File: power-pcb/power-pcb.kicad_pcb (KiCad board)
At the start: 2 copper layers, 75 x 55 mm, 41 parts, among them J1 Network Connector, J2 STDC14, SW1 SW_Push, U1 LD39050PU33R, U2 STM32G474RBT6, U3 SN65HVD230, Y1 8MHz

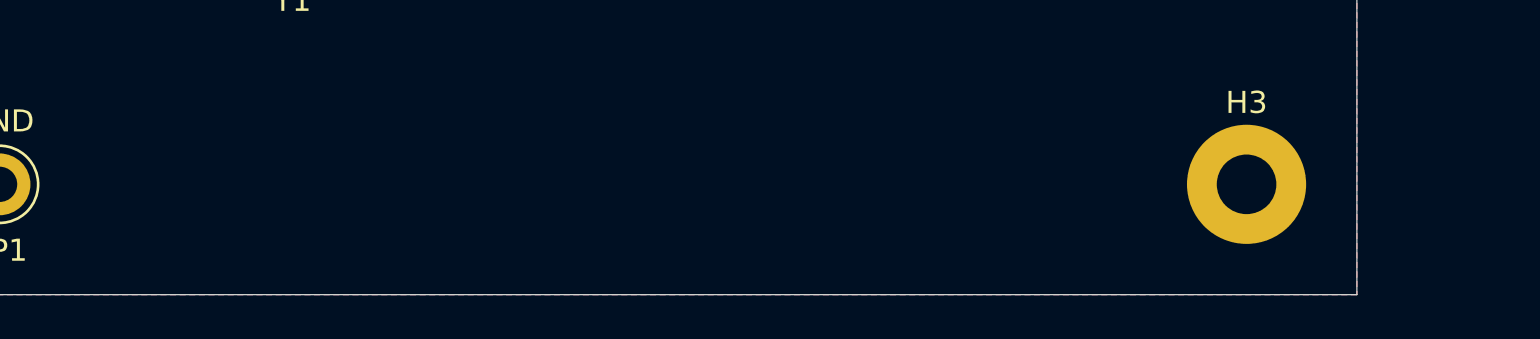
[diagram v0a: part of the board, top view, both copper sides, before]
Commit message: power-pcb: update project metadata
Also added project code, name and version to silkscreen in the board
layout.
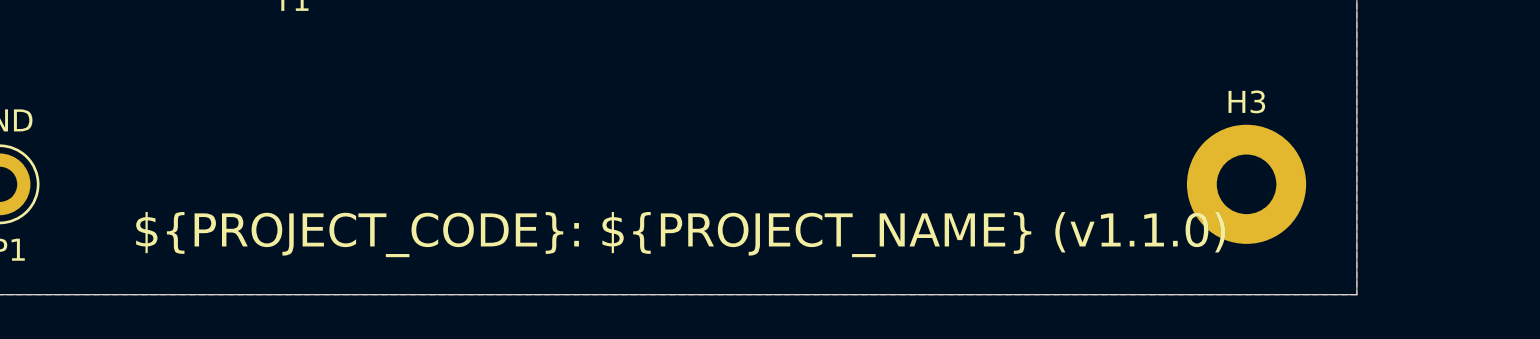
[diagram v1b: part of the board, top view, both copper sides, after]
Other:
- board text added: "${PROJECT_CODE}: ${PROJECT_NAME} (${REVISION})"
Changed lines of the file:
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@@
 	(paper "A4")
 	(title_block
-		(title "Base board layout")
-		(date "2025-04-06")
-		(rev "v1.0.0")
+		(title "Board layout")
+		(date "2026-03-28")
+		(rev "v1.1.0")
 	)
 	(layers
@@
 		)
 	)
-	(property "AUTHOR" "Guillaume Chénier")
-	(property "CONTRIBUTORS" "Eliot F., Wilfred P.")
-	(property "PROJECT_CODE" "TEM.00")
-	(property "PROJECT_NAME" "STM32 PCB Template")
-	(property "REVIEWERS" "Eliot F.")
+	(property "AUTHOR" "Daphné H.")
+	(property "CONTRIBUTORS" "")
+	(property "PROJECT_CODE" "PCB.04")
+	(property "PROJECT_NAME" "Power Control PCB")
+	(property "REVIEWERS" "")
 	(net 0 "")
 	(net 1 "GND")
@@
 		(layer "Edge.Cuts")
 	)
+	(gr_text "${PROJECT_CODE}: ${PROJECT_NAME} (${REVISION})"
+		(at 209.5 74.5 0)
+		(layer "F.SilkS")
+		(effects
+			(font
+				(size 1.5 1.5)
+				(thickness 0.1875)
+			)
+			(justify left bottom)
+		)
+	)
 	(segment

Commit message: power-pcb: re-annotate schematic and start board
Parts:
- added C18: 10n, Capacitor_SMD:C_0402_1005Metric_Pad0.74x0.62mm_HandSolder, F.Cu at (94.4, 134.0)
- added C19: 100n, Capacitor_SMD:C_0603_1608Metric_Pad1.08x0.95mm_HandSolder, F.Cu at (89.9, 122.3)
- added C20: 100n, Capacitor_SMD:C_0603_1608Metric_Pad1.08x0.95mm_HandSolder, F.Cu at (89.9, 124.8)
- added C21: 100n, Capacitor_SMD:C_0603_1608Metric_Pad1.08x0.95mm_HandSolder, F.Cu at (89.9, 127.3)
- added C22: 2.2u, Capacitor_SMD:C_0805_2012Metric_Pad1.18x1.45mm_HandSolder, F.Cu at (82.0, 134.5)
- added C23: 2.2u, Capacitor_SMD:C_0805_2012Metric_Pad1.18x1.45mm_HandSolder, F.Cu at (82.0, 137.5)
- added C24: 2.2u, Capacitor_SMD:C_0805_2012Metric_Pad1.18x1.45mm_HandSolder, F.Cu at (82.0, 140.6)
- added C25: 30p, Capacitor_SMD:C_0603_1608Metric_Pad1.08x0.95mm_HandSolder, F.Cu at (89.9, 129.8)
- added C26: 30p, Capacitor_SMD:C_0603_1608Metric_Pad1.08x0.95mm_HandSolder, F.Cu at (94.2, 117.3)
- added C27: 100n, Capacitor_SMD:C_0603_1608Metric_Pad1.08x0.95mm_HandSolder, F.Cu at (101.0, 64.7)
- added C28: 100n, Capacitor_SMD:C_0603_1608Metric_Pad1.08x0.95mm_HandSolder, F.Cu at (101.0, 67.2)
- added C29: 100n, Capacitor_SMD:C_0603_1608Metric_Pad1.08x0.95mm_HandSolder, F.Cu at (101.0, 69.7)
- added C30: 100n, Capacitor_SMD:C_0603_1608Metric_Pad1.08x0.95mm_HandSolder, F.Cu at (101.0, 72.2)
- added C31: 100n, Capacitor_SMD:C_0603_1608Metric_Pad1.08x0.95mm_HandSolder, F.Cu at (101.0, 74.7)
- added C32: 100n, Capacitor_SMD:C_0603_1608Metric_Pad1.08x0.95mm_HandSolder, F.Cu at (101.0, 77.2)
- added C33: 100n, Capacitor_SMD:C_0603_1608Metric_Pad1.08x0.95mm_HandSolder, F.Cu at (101.0, 79.8)
- added C34: 100n, Capacitor_SMD:C_0603_1608Metric_Pad1.08x0.95mm_HandSolder, F.Cu at (101.0, 82.3)
- added C35: 100n, Capacitor_SMD:C_0603_1608Metric_Pad1.08x0.95mm_HandSolder, F.Cu at (120.8, 130.3)
- added C36: 10u, Capacitor_SMD:C_1206_3216Metric_Pad1.33x1.80mm_HandSolder, F.Cu at (131.5, 128.3)
- added C37: 10u, Capacitor_SMD:C_1206_3216Metric_Pad1.33x1.80mm_HandSolder, F.Cu at (131.5, 131.6)
- added C38: 100n, Capacitor_SMD:C_0603_1608Metric_Pad1.08x0.95mm_HandSolder, F.Cu at (145.8, 111.0)
- added C39: 100n, Capacitor_SMD:C_0603_1608Metric_Pad1.08x0.95mm_HandSolder, F.Cu at (145.8, 113.5)
- added C40: 10n, Capacitor_SMD:C_0402_1005Metric_Pad0.74x0.62mm_HandSolder, F.Cu at (167.1, 119.5)
- added C41: 10n, Capacitor_SMD:C_0402_1005Metric_Pad0.74x0.62mm_HandSolder, F.Cu at (167.1, 121.5)
- added C42: 10n, Capacitor_SMD:C_0402_1005Metric_Pad0.74x0.62mm_HandSolder, F.Cu at (167.1, 123.4)
- added C43: 10n, Capacitor_SMD:C_0402_1005Metric_Pad0.74x0.62mm_HandSolder, F.Cu at (167.1, 125.4)
- added C44: 100n, Capacitor_SMD:C_0603_1608Metric_Pad1.08x0.95mm_HandSolder, F.Cu at (145.1, 160.5)
- added C45: 100n, Capacitor_SMD:C_0603_1608Metric_Pad1.08x0.95mm_HandSolder, F.Cu at (145.1, 163.0)
- added C46: 10n, Capacitor_SMD:C_0402_1005Metric_Pad0.74x0.62mm_HandSolder, F.Cu at (166.5, 169.0)
- added C47: 10n, Capacitor_SMD:C_0402_1005Metric_Pad0.74x0.62mm_HandSolder, F.Cu at (166.5, 170.9)
- added C48: 10n, Capacitor_SMD:C_0402_1005Metric_Pad0.74x0.62mm_HandSolder, F.Cu at (166.5, 172.9)
- added C49: 10n, Capacitor_SMD:C_0402_1005Metric_Pad0.74x0.62mm_HandSolder, F.Cu at (166.5, 174.9)
- added C50: 10u, Capacitor_SMD:C_1206_3216Metric_Pad1.33x1.80mm_HandSolder, F.Cu at (82.6, 171.0)
- added C51: 10u, Capacitor_SMD:C_1206_3216Metric_Pad1.33x1.80mm_HandSolder, F.Cu at (82.6, 174.4)
- added C52: 10u, Capacitor_SMD:C_1206_3216Metric_Pad1.33x1.80mm_HandSolder, F.Cu at (82.6, 177.7)
- added C53: 100p, Capacitor_SMD:C_0402_1005Metric_Pad0.74x0.62mm_HandSolder, F.Cu at (107.2, 179.0)
- added C54: 100n, Capacitor_SMD:C_0603_1608Metric_Pad1.08x0.95mm_HandSolder, F.Cu at (87.8, 170.6)
- added C55: 100n, Capacitor_SMD:C_0603_1608Metric_Pad1.08x0.95mm_HandSolder, F.Cu at (87.8, 173.1)
- added C56: 100n, Capacitor_SMD:C_0603_1608Metric_Pad1.08x0.95mm_HandSolder, F.Cu at (129.2, 169.2)
- added C57: 100n, Capacitor_SMD:C_0603_1608Metric_Pad1.08x0.95mm_HandSolder, F.Cu at (129.2, 171.7)
- added C58: 100n, Capacitor_SMD:C_0603_1608Metric_Pad1.08x0.95mm_HandSolder, F.Cu at (129.2, 147.0)
- added C59: 100n, Capacitor_SMD:C_0603_1608Metric_Pad1.08x0.95mm_HandSolder, F.Cu at (129.2, 149.5)
- added C60: 100n, Capacitor_SMD:C_0603_1608Metric_Pad1.08x0.95mm_HandSolder, F.Cu at (158.6, 147.0)
- added C61: 100n, Capacitor_SMD:C_0603_1608Metric_Pad1.08x0.95mm_HandSolder, F.Cu at (158.6, 149.5)
- added C62: 100n, Capacitor_SMD:C_0603_1608Metric_Pad1.08x0.95mm_HandSolder, F.Cu at (29.7, 67.4)
- added C63: 100n, Capacitor_SMD:C_0603_1608Metric_Pad1.08x0.95mm_HandSolder, F.Cu at (29.7, 70.0)
- added C64: 100n, Capacitor_SMD:C_0603_1608Metric_Pad1.08x0.95mm_HandSolder, F.Cu at (29.7, 72.5)
- added C65: 100n, Capacitor_SMD:C_0603_1608Metric_Pad1.08x0.95mm_HandSolder, F.Cu at (29.7, 75.0)
- added C66: 100n, Capacitor_SMD:C_0603_1608Metric_Pad1.08x0.95mm_HandSolder, F.Cu at (29.7, 77.5)
- added C67: 100n, Capacitor_SMD:C_0603_1608Metric_Pad1.08x0.95mm_HandSolder, F.Cu at (29.7, 80.0)
- added D10: YELLOW, Exocet:LED_0805_2012Metric_With_Annotations, F.Cu at (98.6, 140.5)
- added D11: SMF5.0A, Diode_SMD:D_SOD-123F, F.Cu at (88.4, 178.5)
- added D12: SMF5.0A, Diode_SMD:D_SOD-123F, F.Cu at (91.6, 85.7)
- added D13: SMF5.0A, Diode_SMD:D_SOD-123F, F.Cu at (91.6, 89.0)
- added D14: SMF24CA, Diode_SMD:D_SOD-123F, F.Cu at (91.6, 92.4)
- added D15: SMF24CA, Diode_SMD:D_SOD-123F, F.Cu at (91.6, 95.7)
- added D16: SMF28A, Diode_SMD:D_SMF, F.Cu at (91.7, 99.1)
- added D17: SMF28A, Diode_SMD:D_SMF, F.Cu at (91.7, 102.4)
- added D18: 1N4148, Diode_THT:D_DO-35_SOD27_P7.62mm_Horizontal, F.Cu at (46.5, 98.9)
- added D19: 1N4148, Diode_THT:D_DO-35_SOD27_P7.62mm_Horizontal, F.Cu at (46.5, 102.4)
- added D20: BZX79-C4V7, Diode_THT:D_DO-35_SOD27_P7.62mm_Horizontal, F.Cu at (46.5, 106.0)
- added D3: GREEN, Exocet:LED_0805_2012Metric_With_Annotations, F.Cu at (70.6, 120.3)
- added D4: GREEN, Exocet:LED_0805_2012Metric_With_Annotations, F.Cu at (70.6, 123.4)
- added D5: GREEN, Exocet:LED_0805_2012Metric_With_Annotations, F.Cu at (70.6, 126.4)
- added D6: SMF24CA, Diode_SMD:D_SOD-123F, F.Cu at (72.4, 140.6)
- added D7: SMF24CA, Diode_SMD:D_SOD-123F, F.Cu at (72.4, 143.9)
- added D8: SS34, Diode_SMD:D_SMA, F.Cu at (63.1, 135.8)
- added D9: SMF5.0A, Diode_SMD:D_SOD-123F, F.Cu at (72.4, 147.3)
- added F2: 5A, Exocet:Fuseholder_Littelfuse_Combined, F.Cu at (39.7, 114.3)
- added F3: RUEF110, Fuse:Fuse_Littelfuse_395Series, F.Cu at (34.3, 147.7)
- added F4: 10A, Exocet:Fuseholder_Littelfuse_Combined, F.Cu at (57.1, 70.7)
- added J10: USB_A, Connector_USB:USB_A_Molex_67643_Horizontal, F.Cu at (98.2, 147.4)
- added J11: Screw_Terminal_01x04, Exocet:Wuerth_Term_Blk_4pos_Side_Entry_5mm, F.Cu at (122.8, 163.3)
- added J12: Screw_Terminal_01x04, Exocet:Wuerth_Term_Blk_4pos_Side_Entry_5mm, F.Cu at (122.8, 141.1)
- added J13: Screw_Terminal_01x04, Exocet:Wuerth_Term_Blk_4pos_Side_Entry_5mm, F.Cu at (152.3, 141.1)
- added J14: Screw_Terminal_01x02, Exocet:Wuerth_Term_Blk_2pos_Side_Entry_5mm, F.Cu at (31.8, 90.4)
- added J15: Screw_Terminal_01x06, Exocet:Wuerth_Term_Blk_6pos_Side_Entry_5mm, F.Cu at (67.9, 46.1)
- added J16: Screw_Terminal_01x02, Exocet:Wuerth_Term_Blk_2pos_Side_Entry_5mm, F.Cu at (31.8, 99.1)
- added J17: Screw_Terminal_01x04, Exocet:Wuerth_Term_Blk_4pos_Side_Entry_5mm, F.Cu at (71.4, 79.4)
- added J18: Screw_Terminal_01x03, Exocet:Wuerth_Term_Blk_3pos_Side_Entry_5mm, F.Cu at (67.9, 54.9)
- added J3: STDC14, Connector_PinHeader_1.27mm:PinHeader_2x07_P1.27mm_Vertical_SMD, F.Cu at (36.7, 155.9)
- added J4: USB_C_Receptacle_USB2.0_16P, Connector_USB:USB_C_Receptacle_GCT_USB4085, F.Cu at (52.0, 150.1)
- added J5: RA25S, Connector_Dsub:DSUB-25_Socket_Horizontal_P2.77x2.84mm_EdgePinOffset7.70mm_Housed_MountingHolesOffset9.12mm, F.Cu at (143.0, 45.3)
- added J6: JST PH, Connector_JST:JST_PH_S3B-PH-K_1x03_P2.00mm_Horizontal, F.Cu at (121.6, 112.1)
- added J7: JST PH, Connector_JST:JST_PH_S3B-PH-K_1x03_P2.00mm_Horizontal, F.Cu at (121.6, 121.8)
- added J8: Screw_Terminal_01x03, Exocet:Wuerth_Term_Blk_3pos_Side_Entry_5mm, F.Cu at (152.2, 113.9)
- added J9: Screw_Terminal_01x03, Exocet:Wuerth_Term_Blk_3pos_Side_Entry_5mm, F.Cu at (151.6, 163.3)
- added JP1: Jumper_3_Bridged12, Connector_PinHeader_2.54mm:PinHeader_1x03_P2.54mm_Vertical, F.Cu at (51.5, 141.2)
- added JP2: Jumper_3_Bridged12, Connector_PinHeader_2.54mm:PinHeader_1x03_P2.54mm_Vertical, F.Cu at (56.1, 141.2)
- added JP3: Jumper_3_Bridged12, Connector_PinHeader_2.54mm:PinHeader_1x03_P2.54mm_Vertical, F.Cu at (60.7, 141.2)
- added JP4: Jumper_3_Bridged12, Connector_PinHeader_2.54mm:PinHeader_1x03_P2.54mm_Vertical, F.Cu at (109.2, 132.8)
- added JP5: SolderJumper_2_Open, Jumper:SolderJumper-2_P1.3mm_Open_RoundedPad1.0x1.5mm, F.Cu at (107.7, 173.0)
- added JP6: SolderJumper_2_Bridged, Jumper:SolderJumper-2_P1.3mm_Bridged_Pad1.0x1.5mm, F.Cu at (91.0, 105.9)
- added L1: 10u, Inductor_THT:L_Radial_D8.7mm_P5.00mm_Fastron_07HCP, F.Cu at (34.5, 124.0)
- added L2: 10u, Inductor_THT:L_Radial_D8.7mm_P5.00mm_Fastron_07HCP, F.Cu at (34.5, 134.2)
- added L3: GZ2012D101TF, Inductor_SMD:L_0805_2012Metric_Pad1.05x1.20mm_HandSolder, F.Cu at (72.1, 150.3)
- added L4: GZ2012D101TF, Inductor_SMD:L_0805_2012Metric_Pad1.05x1.20mm_HandSolder, F.Cu at (158.8, 130.0)
- added L5: GZ2012D101TF, Inductor_SMD:L_0805_2012Metric_Pad1.05x1.20mm_HandSolder, F.Cu at (158.8, 132.7)
- added L6: GZ2012D101TF, Inductor_SMD:L_0805_2012Metric_Pad1.05x1.20mm_HandSolder, F.Cu at (158.2, 179.4)
- added L7: GZ2012D101TF, Inductor_SMD:L_0805_2012Metric_Pad1.05x1.20mm_HandSolder, F.Cu at (158.2, 182.2)
- added L8: GZ2012D101TF, Inductor_SMD:L_0805_2012Metric_Pad1.05x1.20mm_HandSolder, F.Cu at (108.0, 169.8)
- added Q1: AO3400A, Package_TO_SOT_SMD:SOT-23, F.Cu at (71.8, 68.4)
- added Q2: AO3400A, Package_TO_SOT_SMD:SOT-23, F.Cu at (71.8, 72.9)
- added Q3: AO3400A, Package_TO_SOT_SMD:SOT-23, F.Cu at (76.7, 68.4)
- added Q4: AO3400A, Package_TO_SOT_SMD:SOT-23, F.Cu at (76.7, 72.9)
- added Q5: AO3400A, Package_TO_SOT_SMD:SOT-23, F.Cu at (81.6, 68.4)
- added Q6: AO3400A, Package_TO_SOT_SMD:SOT-23, F.Cu at (81.6, 72.9)
- added Q7: AO3400A, Package_TO_SOT_SMD:SOT-23, F.Cu at (86.5, 68.4)
- added Q8: AO3400A, Package_TO_SOT_SMD:SOT-23, F.Cu at (86.5, 72.9)
- added R10: 2.7k, Resistor_SMD:R_0603_1608Metric_Pad0.98x0.95mm_HandSolder, F.Cu at (94.2, 119.8)
- added R11: 2.7k, Resistor_SMD:R_0603_1608Metric_Pad0.98x0.95mm_HandSolder, F.Cu at (94.2, 122.3)
- added R12: 47, Resistor_SMD:R_0603_1608Metric_Pad0.98x0.95mm_HandSolder, F.Cu at (94.2, 124.8)
- added R13: 10k, Resistor_SMD:R_0603_1608Metric_Pad0.98x0.95mm_HandSolder, F.Cu at (94.2, 127.3)
- added R14: 1k, Resistor_SMD:R_0402_1005Metric_Pad0.72x0.64mm_HandSolder, F.Cu at (94.4, 139.6)
- added R15: 2.2k, Resistor_SMD:R_0603_1608Metric_Pad0.98x0.95mm_HandSolder, F.Cu at (120.8, 132.8)
- added R16: 82k, Resistor_SMD:R_0603_1608Metric_Pad0.98x0.95mm_HandSolder, F.Cu at (145.8, 116.0)
- added R17: 6.8k, Resistor_SMD:R_0603_1608Metric_Pad0.98x0.95mm_HandSolder, F.Cu at (145.8, 118.6)
- added R18: 10k, Resistor_SMD:R_0603_1608Metric_Pad0.98x0.95mm_HandSolder, F.Cu at (145.8, 121.1)
- added R19: 10k, Resistor_SMD:R_0603_1608Metric_Pad0.98x0.95mm_HandSolder, F.Cu at (145.8, 123.6)
- added R20: 2.7k, Resistor_SMD:R_0603_1608Metric_Pad0.98x0.95mm_HandSolder, F.Cu at (145.8, 126.1)
- added R21: 2.7k, Resistor_SMD:R_0603_1608Metric_Pad0.98x0.95mm_HandSolder, F.Cu at (145.8, 128.6)
- added R22: 82k, Resistor_SMD:R_0603_1608Metric_Pad0.98x0.95mm_HandSolder, F.Cu at (145.1, 165.5)
- added R23: 6.8k, Resistor_SMD:R_0603_1608Metric_Pad0.98x0.95mm_HandSolder, F.Cu at (145.1, 168.0)
- added R24: 10k, Resistor_SMD:R_0603_1608Metric_Pad0.98x0.95mm_HandSolder, F.Cu at (145.1, 170.5)
- added R25: 10k, Resistor_SMD:R_0603_1608Metric_Pad0.98x0.95mm_HandSolder, F.Cu at (145.1, 173.0)
- added R26: 2.7k, Resistor_SMD:R_0603_1608Metric_Pad0.98x0.95mm_HandSolder, F.Cu at (145.1, 175.5)
- added R27: 2.7k, Resistor_SMD:R_0603_1608Metric_Pad0.98x0.95mm_HandSolder, F.Cu at (145.1, 178.0)
- added R28: 10k, Resistor_SMD:R_0603_1608Metric_Pad0.98x0.95mm_HandSolder, F.Cu at (87.8, 175.6)
- added R29: 10k, Resistor_SMD:R_0603_1608Metric_Pad0.98x0.95mm_HandSolder, F.Cu at (29.7, 82.5)
- added R30: 10k, Resistor_SMD:R_0603_1608Metric_Pad0.98x0.95mm_HandSolder, F.Cu at (29.7, 85.0)
- added R31: 3.6k, Resistor_SMD:R_0603_1608Metric_Pad0.98x0.95mm_HandSolder, F.Cu at (34.0, 67.4)
- added R32: 120, Resistor_THT:R_Axial_DIN0309_L9.0mm_D3.2mm_P12.70mm_Horizontal, F.Cu at (82.6, 53.1)
- added R33: 120, Resistor_THT:R_Axial_DIN0309_L9.0mm_D3.2mm_P12.70mm_Horizontal, F.Cu at (82.6, 57.9)
- added R34: 6.8k, Resistor_SMD:R_0603_1608Metric_Pad0.98x0.95mm_HandSolder, F.Cu at (34.0, 70.0)
- added R35: 10k, Resistor_SMD:R_0603_1608Metric_Pad0.98x0.95mm_HandSolder, F.Cu at (34.0, 72.5)
- added R36: 10k, Resistor_SMD:R_0603_1608Metric_Pad0.98x0.95mm_HandSolder, F.Cu at (34.0, 75.0)
- added R37: 10k, Resistor_SMD:R_0603_1608Metric_Pad0.98x0.95mm_HandSolder, F.Cu at (34.0, 77.5)
- added R38: 10k, Resistor_SMD:R_0603_1608Metric_Pad0.98x0.95mm_HandSolder, F.Cu at (34.0, 80.0)
- added R39: 10k, Resistor_SMD:R_0603_1608Metric_Pad0.98x0.95mm_HandSolder, F.Cu at (34.0, 82.5)
- added R40: 10k, Resistor_SMD:R_0603_1608Metric_Pad0.98x0.95mm_HandSolder, F.Cu at (34.0, 85.0)
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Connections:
- C1 pad 1: +5V -> Net-(U1-BOOT)
- C1 pad 2: GND -> Net-(D2-K)
- C10 pad 1: +3.3V -> +5V
- C15 pad 1: /STM32 Base Layout/OSC_IN -> +3.3V
- C16 pad 1: /STM32 Base Layout/OSC_OUT -> GND
- C16 pad 2: GND -> +3.3V
- C17 pad 1: GND -> +3.3V
- C17 pad 2: /STM32 Base Layout/T_NRST -> GND
- C2 pad 1: GND -> +24V
- C2 pad 2: +3.3V -> GND
- C3 pad 1: GND -> Net-(C3-Pad1)
- C3 pad 2: +3.3V -> GND
- C4 pad 1: +5V -> Net-(C3-Pad1)
- C5 pad 1: +3.3V -> +24V
- C6 pad 1: +3.3V -> Net-(D9-K)
- C7 pad 1: +3.3V -> Net-(C7-Pad1)
- C9 pad 1: +3.3V -> +5V
- D1 pad 1: GND -> +24V
- D1 pad 2: Net-(D1-A) -> GND
- D2 pad 1: GND -> Net-(D2-K)
- D2 pad 2: Net-(D2-A) -> GND
- F1 pad 1: Net-(J1-+5V) -> Net-(C3-Pad1)
- F1 pad 2: +5V -> /Non-Isolated Interfaces and Power/5V_NETWORK
- J1 pad 1: +24V -> Net-(J1-+24V)
- J1 pad 2: Net-(J1-+5V) -> unconnected-(J1-+5V-Pad2)
- J1 pad 3: /STM32 Base Layout/CAN_L -> /Non-Isolated Interfaces and Power/CAN_L
- J1 pad 4: /STM32 Base Layout/CAN_H -> /Non-Isolated Interfaces and Power/CAN_H
- J2 pad 1: unconnected-(J2-NC-Pad1) -> +24V
- J2 pad 2: unconnected-(J2-NC-Pad2) -> GND
- R1 pad 1: Net-(U2-PB8) -> Net-(C3-Pad1)
- R1 pad 2: GND -> Net-(U1-VSENSE)
- R2 pad 1: Net-(U2-PA15) -> +24V
- R2 pad 2: /STM32 Base Layout/T_JTDI -> Net-(D3-A)
- R3 pad 1: Net-(U3-Rs) -> +5V
- R3 pad 2: GND -> Net-(D4-A)
- R4 pad 2: Net-(D1-A) -> Net-(D5-A)
- R5 pad 1: /STM32 Base Layout/STATUS_LED -> Net-(U1-VSENSE)
- R5 pad 2: Net-(D2-A) -> Net-(R5-Pad2)
- SW1 pad 1: /STM32 Base Layout/T_NRST -> /Non-Isolated Interfaces and Power/~{RST}
- TP1 pad 1: GND -> Net-(C3-Pad1)
- TP2 pad 1: /STM32 Base Layout/CAN_RX -> +24V
- TP3 pad 1: +5V -> GND
- TP4 pad 1: /STM32 Base Layout/CAN_TX -> Net-(U1-VSENSE)
- TP5 pad 1: +3.3V -> Net-(C7-Pad1)
- U1 pad 1: +5V -> Net-(U1-BOOT)
- U1 pad 2: GND -> unconnected-(U1-NC-Pad2)
- U1 pad 4: +3.3V -> Net-(U1-VSENSE)
- U1 pad 6: +5V -> GND
- U1 pad 7: GND -> +24V
- U2 pad 1: +3.3V -> Net-(U2-D+_in)
- U2 pad 2: unconnected-(U2-PC13-Pad2) -> Net-(U2-D-_in)
- U2 pad 3: unconnected-(U2-PC14-Pad3) -> GND
- U2 pad 5: /STM32 Base Layout/OSC_IN -> /Non-Isolated Interfaces and Power/PC_D-
- U2 pad 6: /STM32 Base Layout/OSC_OUT -> /Non-Isolated Interfaces and Power/PC_D+
- U3 pad 1: /STM32 Base Layout/CAN_TX -> GND
- U3 pad 2: GND -> +3.3V
- U3 pad 3: +3.3V -> +5V
- Y1 pad 1: /STM32 Base Layout/OSC_IN -> /STM32 Microcontroller/OSC_IN
- Y1 pad 2: /STM32 Base Layout/OSC_OUT -> /STM32 Microcontroller/OSC_OUT
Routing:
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- removed copper zone on B.Cu, net +3.3V
- removed copper zone on F.Cu, net GND
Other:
- board outline removed

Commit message: power-pcb: fix schematic after review
- Add footprint for resitive load for the RECOM
- Add Opamps when useful
- Add capacitor and change some footprint sizes
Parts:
- removed R33: 120, Resistor_THT:R_Axial_DIN0309_L9.0mm_D3.2mm_P12.70mm_Horizontal
- C2: value 10u -> 100n; footprint Capacitor_SMD:C_1206_3216Metric_Pad1.33x1.80mm_HandSolder -> Capacitor_SMD:C_0603_1608Metric_Pad1.08x0.95mm_HandSolder
- F3, JP5, TP57, TP59: moved to B.Cu
- moved H2 171.0 mm to (123.5, 30.0)
- moved J13 137.6 mm to (30.5, 77.0), turned to -90 degrees
- moved H1 136.9 mm to (31.0, 30.0)
- moved C44 134.3 mm to (276.2, 131.5)
- moved C45 134.3 mm to (276.2, 134.0)
- moved C60 134.3 mm to (289.7, 118.0)
- moved C61 134.3 mm to (289.7, 120.5)
- moved R22 134.3 mm to (276.2, 136.5)
- moved R23 134.3 mm to (276.2, 139.0)
- moved R24 134.3 mm to (276.2, 141.5)
- moved R25 134.3 mm to (276.2, 144.0)
- moved R26 134.3 mm to (276.2, 146.5)
- moved R27 134.3 mm to (276.2, 149.1)
- moved U25 134.3 mm to (294.5, 119.2)
- moved C16 134.3 mm to (213.1, 102.5)
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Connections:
- J17 pad 1: +24V -> /Relay Board Connection/+24V_CONTACTORS
- J17 pad 4: /Relay Board Connection/+24V_CONTACTORS -> +24V
- TP57 pad 1: Net-(U18-D+_out) -> Net-(U18-D+_in)
- TP59 pad 1: Net-(U18-D-_out) -> Net-(U18-D-_in)
- U18 pad 1: Net-(J10-D+) -> Net-(U18-D+_in)
- U18 pad 2: Net-(J10-D-) -> Net-(U18-D-_in)
- U18 pad 5: Net-(U18-D-_out) -> Net-(J10-D-)
- U18 pad 6: Net-(U18-D+_out) -> Net-(J10-D+)
- U19 pad 6: Net-(U18-D-_out) -> Net-(U18-D-_in)
- U19 pad 7: Net-(U18-D+_out) -> Net-(U18-D+_in)
- U28 pad 1: Net-(D18-A) -> Net-(J16-Pin_2)
- U28 pad 2: Net-(J16-Pin_2) -> Net-(D18-A)
- U28 pad 3: Net-(F4-Pad1) -> unconnected-(U28-Pad3)
- U28 pad 4: unconnected-(U28-Pad4) -> Net-(F4-Pad1)
- U29 pad 1: Net-(D19-A) -> Net-(J17-Pin_2)
- U29 pad 2: Net-(J17-Pin_3) -> Net-(D19-A)
- U29 pad 3: Net-(J17-Pin_2) -> unconnected-(U29-Pad3)
- U29 pad 4: unconnected-(U29-Pad4) -> Net-(J17-Pin_3)
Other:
- board outline added: 102.5 x 150 mm
- board text added: "+24V"

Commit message: power-pcb: work on part placement and JLCPCB DNP
Some of the components that were recentlt added had not been marked as
DNP for JLCPCB yet, this is now done.
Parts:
- removed the C62 at (160.8, 38.5)
- removed the D14 at (222.6, 63.4)
- removed the D15 at (222.6, 66.7)
- removed the D16 at (222.8, 70.1)
- removed the D17 at (222.8, 73.4)
- removed the J15 at (65.5, 34.0)
- removed the L2 at (165.6, 105.2)
- removed the R16 at (276.8, 87.0)
- removed the R22 at (276.2, 136.5)
- removed the TP76 at (212.3, 62.6)
- removed the TP79 at (222.1, 39.2)
- removed the TP80 at (212.3, 67.6)
- removed the TP82 at (189.3, 62.2)
- removed the U27 at (198.9, 33.9)
- added C2: 2.2u, Capacitor_SMD:C_0805_2012Metric_Pad1.18x1.45mm_HandSolder, F.Cu at (88.5, 137.7)
- added C41: 100n, Capacitor_SMD:C_0402_1005Metric_Pad0.74x0.62mm_HandSolder, F.Cu at (182.9, -27.2)
- added C48: 100n, Capacitor_SMD:C_0402_1005Metric_Pad0.74x0.62mm_HandSolder, F.Cu at (175.0, 15.9)
- added C6: 2.2u, Capacitor_SMD:C_0805_2012Metric_Pad1.18x1.45mm_HandSolder, F.Cu at (69.8, 130.2)
- added C67: 100n, Capacitor_SMD:C_0402_1005Metric_Pad0.74x0.62mm_HandSolder, F.Cu at (182.9, -16.6)
- added C72: 100n, Capacitor_SMD:C_0402_1005Metric_Pad0.74x0.62mm_HandSolder, F.Cu at (168.9, -16.3)
- added D18: SMF24CA, Diode_SMD:D_SOD-123F, F.Cu at (168.0, -26.3)
- added D19: SMF24CA, Diode_SMD:D_SOD-123F, F.Cu at (168.0, -23.0)
- added D20: SMF28A, Diode_SMD:D_SMF, F.Cu at (162.3, -26.3)
- added D21: SMF28A, Diode_SMD:D_SMF, F.Cu at (162.3, -23.0)
- added D9: SMF28A, Diode_SMD:D_SMF, F.Cu at (78.5, 146.2)
- added F3: 2A, Exocet:Fuseholder_Littelfuse_Combined, F.Cu at (84.7, 154.0)
- added J18: Screw_Terminal_01x06, Exocet:Wuerth_Term_Blk_6pos_Side_Entry_5mm, F.Cu at (65.4, 34.0)
- added L3: GZ2012D101TF, Inductor_SMD:L_0805_2012Metric_Pad1.05x1.20mm_HandSolder, F.Cu at (45.5, 99.0)
- added R15: 100, Resistor_SMD:R_0603_1608Metric_Pad0.98x0.95mm_HandSolder, F.Cu at (69.5, 78.0)
- added R19: 250, Resistor_THT:R_Axial_DIN0309_L9.0mm_D3.2mm_P12.70mm_Horizontal, F.Cu at (140.1, 16.4)
- added R20: 56k, Resistor_SMD:R_0603_1608Metric_Pad0.98x0.95mm_HandSolder, F.Cu at (175.1, -35.5)
- added R21: 5.1k, Resistor_SMD:R_0402_1005Metric_Pad0.72x0.64mm_HandSolder, F.Cu at (182.9, -29.2)
- added R25: 10k, Resistor_SMD:R_0603_1608Metric_Pad0.98x0.95mm_HandSolder, F.Cu at (175.1, -30.5)
- added R28: 100, Resistor_SMD:R_0603_1608Metric_Pad0.98x0.95mm_HandSolder, F.Cu at (175.1, -28.0)
- added R29: 56k, Resistor_SMD:R_0603_1608Metric_Pad0.98x0.95mm_HandSolder, F.Cu at (167.1, 7.58)
- added R30: 5.1k, Resistor_SMD:R_0402_1005Metric_Pad0.72x0.64mm_HandSolder, F.Cu at (175.0, 13.9)
- added R34: 10k, Resistor_SMD:R_0603_1608Metric_Pad0.98x0.95mm_HandSolder, F.Cu at (167.1, 12.6)
- added R37: 100, Resistor_SMD:R_0603_1608Metric_Pad0.98x0.95mm_HandSolder, F.Cu at (167.1, 15.1)
- added R38: 250, Resistor_THT:R_Axial_DIN0309_L9.0mm_D3.2mm_P12.70mm_Horizontal, B.Cu at (28.5, 97.5)
- added R39: 250, Resistor_THT:R_Axial_DIN0309_L9.0mm_D3.2mm_P12.70mm_Horizontal, F.Cu at (166.5, -2.79)
- added R40: 250, Resistor_THT:R_Axial_DIN0309_L9.0mm_D3.2mm_P12.70mm_Horizontal, F.Cu at (166.5, 1.96)
- added R42: 10k, Resistor_SMD:R_0603_1608Metric_Pad0.98x0.95mm_HandSolder, F.Cu at (175.1, -16.3)
- added R46: 10k, Resistor_SMD:R_0603_1608Metric_Pad0.98x0.95mm_HandSolder, F.Cu at (175.1, -13.8)
- added R69: 120, Resistor_THT:R_Axial_DIN0309_L9.0mm_D3.2mm_P12.70mm_Horizontal, F.Cu at (140.1, -25.6)
- added R70: 120, Resistor_THT:R_Axial_DIN0309_L9.0mm_D3.2mm_P12.70mm_Horizontal, F.Cu at (140.1, -20.9)
- added R9: 120, Resistor_THT:R_Axial_DIN0309_L9.0mm_D3.2mm_P12.70mm_Horizontal, B.Cu at (117.1, 165.0)
- added TP100: Hole, TestPoint:TestPoint_THTPad_D2.0mm_Drill1.0mm, F.Cu at (165.0, -19.3)
- added TP101: Green, TestPoint:TestPoint_Keystone_5005-5009_Compact, F.Cu at (156.9, -20.4)
- added TP102: Pad, TestPoint:TestPoint_Pad_D1.5mm, F.Cu at (161.2, -16.0)
- added TP42: Hole, TestPoint:TestPoint_THTPad_D2.0mm_Drill1.0mm, F.Cu at (179.3, -28.1)
- added TP49: Hole, TestPoint:TestPoint_THTPad_D2.0mm_Drill1.0mm, F.Cu at (171.3, 14.9)
- added TP98: Yellow, TestPoint:TestPoint_Keystone_5005-5009_Compact, F.Cu at (156.9, -25.5)
- added TP99: Pad, TestPoint:TestPoint_Pad_D1.5mm, F.Cu at (161.2, -19.5)
- added U13: MCP6002T, Package_SO:SOIC-8_3.9x4.9mm_P1.27mm, F.Cu at (173.5, 9.69)
- added U28: MCP6002T, Package_SO:SOIC-8_3.9x4.9mm_P1.27mm, F.Cu at (177.1, -20.8)
- added U33: TJA1050, Package_SO:SOIC-8_3.9x4.9mm_P1.27mm, F.Cu at (70.5, 107.2)
- added U9: MCP6002T, Package_SO:SOIC-8_3.9x4.9mm_P1.27mm, F.Cu at (113.6, 223.2)
- C10: renamed from C8; footprint Capacitor_SMD:C_0603_1608Metric_Pad1.08x0.95mm_HandSolder -> Capacitor_SMD:C_0402_1005Metric_Pad0.74x0.62mm_HandSolder
- C11: renamed from C9; footprint Capacitor_SMD:C_0603_1608Metric_Pad1.08x0.95mm_HandSolder -> Capacitor_SMD:C_0402_1005Metric_Pad0.74x0.62mm_HandSolder
- C14: renamed from C12; footprint Capacitor_SMD:C_0603_1608Metric_Pad1.08x0.95mm_HandSolder -> Capacitor_SMD:C_0402_1005Metric_Pad0.74x0.62mm_HandSolder
- C15: renamed from C13; footprint Capacitor_SMD:C_0603_1608Metric_Pad1.08x0.95mm_HandSolder -> Capacitor_SMD:C_0402_1005Metric_Pad0.74x0.62mm_HandSolder
- C18: renamed from C15; footprint Capacitor_SMD:C_0603_1608Metric_Pad1.08x0.95mm_HandSolder -> Capacitor_SMD:C_0402_1005Metric_Pad0.74x0.62mm_HandSolder
- C21: renamed from C19; footprint Capacitor_SMD:C_0603_1608Metric_Pad1.08x0.95mm_HandSolder -> Capacitor_SMD:C_0402_1005Metric_Pad0.74x0.62mm_HandSolder
- C22: renamed from C20; footprint Capacitor_SMD:C_0603_1608Metric_Pad1.08x0.95mm_HandSolder -> Capacitor_SMD:C_0402_1005Metric_Pad0.74x0.62mm_HandSolder
- C23: renamed from C21; footprint Capacitor_SMD:C_0603_1608Metric_Pad1.08x0.95mm_HandSolder -> Capacitor_SMD:C_0402_1005Metric_Pad0.74x0.62mm_HandSolder
- C29: renamed from C27; footprint Capacitor_SMD:C_0603_1608Metric_Pad1.08x0.95mm_HandSolder -> Capacitor_SMD:C_0402_1005Metric_Pad0.74x0.62mm_HandSolder
- C3: renamed from C2; footprint Capacitor_SMD:C_0603_1608Metric_Pad1.08x0.95mm_HandSolder -> Capacitor_SMD:C_0402_1005Metric_Pad0.74x0.62mm_HandSolder
- C30: renamed from C28; footprint Capacitor_SMD:C_0603_1608Metric_Pad1.08x0.95mm_HandSolder -> Capacitor_SMD:C_0402_1005Metric_Pad0.74x0.62mm_HandSolder
- C31: renamed from C29; footprint Capacitor_SMD:C_0603_1608Metric_Pad1.08x0.95mm_HandSolder -> Capacitor_SMD:C_0402_1005Metric_Pad0.74x0.62mm_HandSolder
- C32: renamed from C30; footprint Capacitor_SMD:C_0603_1608Metric_Pad1.08x0.95mm_HandSolder -> Capacitor_SMD:C_0402_1005Metric_Pad0.74x0.62mm_HandSolder
- C33: renamed from C31; footprint Capacitor_SMD:C_0603_1608Metric_Pad1.08x0.95mm_HandSolder -> Capacitor_SMD:C_0402_1005Metric_Pad0.74x0.62mm_HandSolder
- C34: renamed from C32; footprint Capacitor_SMD:C_0603_1608Metric_Pad1.08x0.95mm_HandSolder -> Capacitor_SMD:C_0402_1005Metric_Pad0.74x0.62mm_HandSolder
- C35: renamed from C33; footprint Capacitor_SMD:C_0603_1608Metric_Pad1.08x0.95mm_HandSolder -> Capacitor_SMD:C_0402_1005Metric_Pad0.74x0.62mm_HandSolder
- C36: renamed from C34; footprint Capacitor_SMD:C_0603_1608Metric_Pad1.08x0.95mm_HandSolder -> Capacitor_SMD:C_0402_1005Metric_Pad0.74x0.62mm_HandSolder
- C37: renamed from C35; footprint Capacitor_SMD:C_0603_1608Metric_Pad1.08x0.95mm_HandSolder -> Capacitor_SMD:C_0402_1005Metric_Pad0.74x0.62mm_HandSolder
- C4: renamed from C3; footprint Capacitor_THT:CP_Radial_D5.0mm_P2.00mm -> Capacitor_THT:CP_Radial_D8.0mm_P3.50mm
- C40: renamed from C38; footprint Capacitor_SMD:C_0603_1608Metric_Pad1.08x0.95mm_HandSolder -> Capacitor_SMD:C_0402_1005Metric_Pad0.74x0.62mm_HandSolder
- C42: renamed from C39; footprint Capacitor_SMD:C_0603_1608Metric_Pad1.08x0.95mm_HandSolder -> Capacitor_SMD:C_0402_1005Metric_Pad0.74x0.62mm_HandSolder
- C47: renamed from C44; footprint Capacitor_SMD:C_0603_1608Metric_Pad1.08x0.95mm_HandSolder -> Capacitor_SMD:C_0402_1005Metric_Pad0.74x0.62mm_HandSolder
- C49: renamed from C45; footprint Capacitor_SMD:C_0603_1608Metric_Pad1.08x0.95mm_HandSolder -> Capacitor_SMD:C_0402_1005Metric_Pad0.74x0.62mm_HandSolder
- C5: renamed from C4; footprint Capacitor_SMD:C_0603_1608Metric_Pad1.08x0.95mm_HandSolder -> Capacitor_SMD:C_0402_1005Metric_Pad0.74x0.62mm_HandSolder
- C58: renamed from C54; footprint Capacitor_SMD:C_0603_1608Metric_Pad1.08x0.95mm_HandSolder -> Capacitor_SMD:C_0402_1005Metric_Pad0.74x0.62mm_HandSolder
- C59: renamed from C55; footprint Capacitor_SMD:C_0603_1608Metric_Pad1.08x0.95mm_HandSolder -> Capacitor_SMD:C_0402_1005Metric_Pad0.74x0.62mm_HandSolder
- C60: renamed from C56; footprint Capacitor_SMD:C_0603_1608Metric_Pad1.08x0.95mm_HandSolder -> Capacitor_SMD:C_0402_1005Metric_Pad0.74x0.62mm_HandSolder
- C61: renamed from C57; footprint Capacitor_SMD:C_0603_1608Metric_Pad1.08x0.95mm_HandSolder -> Capacitor_SMD:C_0402_1005Metric_Pad0.74x0.62mm_HandSolder
- C62: renamed from C58; footprint Capacitor_SMD:C_0603_1608Metric_Pad1.08x0.95mm_HandSolder -> Capacitor_SMD:C_0402_1005Metric_Pad0.74x0.62mm_HandSolder
- C63: renamed from C59; footprint Capacitor_SMD:C_0603_1608Metric_Pad1.08x0.95mm_HandSolder -> Capacitor_SMD:C_0402_1005Metric_Pad0.74x0.62mm_HandSolder
- C64: renamed from C60; footprint Capacitor_SMD:C_0603_1608Metric_Pad1.08x0.95mm_HandSolder -> Capacitor_SMD:C_0402_1005Metric_Pad0.74x0.62mm_HandSolder
- C65: renamed from C61; footprint Capacitor_SMD:C_0603_1608Metric_Pad1.08x0.95mm_HandSolder -> Capacitor_SMD:C_0402_1005Metric_Pad0.74x0.62mm_HandSolder
- C66: renamed from C63; footprint Capacitor_SMD:C_0603_1608Metric_Pad1.08x0.95mm_HandSolder -> Capacitor_SMD:C_0402_1005Metric_Pad0.74x0.62mm_HandSolder
- C68: renamed from C65; footprint Capacitor_SMD:C_0603_1608Metric_Pad1.08x0.95mm_HandSolder -> Capacitor_SMD:C_0402_1005Metric_Pad0.74x0.62mm_HandSolder
- C69: renamed from C64; footprint Capacitor_SMD:C_0603_1608Metric_Pad1.08x0.95mm_HandSolder -> Capacitor_SMD:C_0402_1005Metric_Pad0.74x0.62mm_HandSolder
- C7: renamed from C5; footprint Capacitor_THT:CP_Radial_D5.0mm_P2.00mm -> Capacitor_THT:CP_Radial_D8.0mm_P3.50mm
- C70: renamed from C67; footprint Capacitor_SMD:C_0603_1608Metric_Pad1.08x0.95mm_HandSolder -> Capacitor_SMD:C_0402_1005Metric_Pad0.74x0.62mm_HandSolder
- C71: renamed from C66; footprint Capacitor_SMD:C_0603_1608Metric_Pad1.08x0.95mm_HandSolder -> Capacitor_SMD:C_0402_1005Metric_Pad0.74x0.62mm_HandSolder
- F1: moved to B.Cu
- L1: value 10u -> 22u; footprint Inductor_THT:L_Radial_D8.7mm_P5.00mm_Fastron_07HCP -> Inductor_THT:L_Axial_L16.0mm_D6.3mm_P5.08mm_Vertical_Fastron_VHBCC
- Q1, Q2, Q3, Q4, Q5, Q6, Q7, Q8: footprint Package_TO_SOT_SMD:SOT-23 -> Package_TO_SOT_SMD:SOT-23_Handsoldering
- R17: value 6.8k -> 250; footprint Resistor_SMD:R_0603_1608Metric_Pad0.98x0.95mm_HandSolder -> Resistor_THT:R_Axial_DIN0309_L9.0mm_D3.2mm_P12.70mm_Horizontal; moved to B.Cu
- R23: value 6.8k -> 10k
- R32: value 120 -> 10k; footprint Resistor_THT:R_Axial_DIN0309_L9.0mm_D3.2mm_P12.70mm_Horizontal -> Resistor_SMD:R_0603_1608Metric_Pad0.98x0.95mm_HandSolder
- TP77: value Pad -> Hole; footprint TestPoint:TestPoint_Pad_D1.5mm -> TestPoint:TestPoint_THTPad_D2.0mm_Drill1.0mm
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- renumbered C10 to C12, C11 to C13, C14 to C16, C16 to C19, C18 to C20, C22 to C24, C23 to C25, C24 to C26, C25 to C27, C26 to C28, C36 to C38, C37 to C39, C40 to C43, C41 to C44, C42 to C45, C43 to C46, C46 to C50, C47 to C51, C48 to C52, C49 to C53, C50 to C54, C51 to C55, C52 to C56, C53 to C57, C6 to C8, C7 to C9, D9 to D10, D10 to D11, D11 to D12, D12 to D13, D13 to D14, D18 to D15, D19 to D16, D20 to D17, F3 to F4, F4 to F5, J18 to J15, L3 to L2, R9 to R10, R10 to R11, R11 to R12, R12 to R13, R13 to R14, R14 to R16, R15 to R18, R18 to R22, R19 to R24, R20 to R26, R21 to R27, R24 to R31, R25 to R33, R26 to R35, R27 to R36, R28 to R41, R29 to R43, R48 to R44, R49 to R45, R30 to R47, R31 to R48, R50 to R49, R34 to R50, R35 to R51, R36 to R53, R37 to R54, R38 to R55, R39 to R56, R40 to R57, R41 to R58, R42 to R59, R43 to R60, R44 to R61, R45 to R62, R46 to R63, R47 to R64, R51 to R65, R53 to R66, R54 to R67, R55 to R68, TP42 to TP43, TP43 to TP44, TP44 to TP45, TP45 to TP46, TP46 to TP47, TP47 to TP48, TP48 to TP50, TP49 to TP51, TP50 to TP52, TP51 to TP53, TP52 to TP54, TP53 to TP55, TP54 to TP56, TP55 to TP57, TP56 to TP58, TP57 to TP59, TP58 to TP60, TP59 to TP61, TP60 to TP62, TP61 to TP63, TP62 to TP64, TP63 to TP65, TP64 to TP66, TP65 to TP67, TP66 to TP68, TP67 to TP69, TP68 to TP70, TP69 to TP71, TP70 to TP72, TP71 to TP73, TP72 to TP74, TP73 to TP75, TP91 to TP76, TP74 to TP78, TP75 to TP79, TP78 to TP80, TP94 to TP82, TP92 to TP91, TP93 to TP92, TP95 to TP93, TP98 to TP94, TP96 to TP95, TP97 to TP96, TP99 to TP97, U9 to U10, U10 to U11, U11 to U12, U12 to U14, U13 to U15, U14 to U16, U15 to U17, U16 to U18, U17 to U19, U18 to U20, U19 to U21, U20 to U22, U21 to U23, U22 to U24, U23 to U25, U24 to U26, U25 to U27, U26 to U29, U28 to U30, U29 to U31, U30 to U32
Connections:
- net /STM32 Microcontroller/DMS_PULSE_CLEAR renamed /STM32 Microcontroller/~{DMS_PULSE_CLEAR}
- C16 pad 1: +3.3V -> GND
- C16 pad 2: GND -> Net-(U5-VDDA)
- C17 pad 1: +3.3V -> GND
- C17 pad 2: GND -> Net-(U5-VDDA)
- C4 pad 1: Net-(C3-Pad1) -> Net-(C4-Pad1)
- C5 pad 1: Net-(C3-Pad1) -> Net-(C4-Pad1)
- C69 pad 1: /Safety Systems/ALARM -> /Safety Systems/~{ALARM}
- D1 pad 1: +24V -> Net-(D1-A1)
- D15 pad 2: Net-(D18-A) -> Net-(D15-A)
- D16 pad 2: Net-(D19-A) -> Net-(D16-A)
- D17 pad 1: /Safety Systems/ALARM -> /Safety Systems/~{ALARM}
- F1 pad 1: Net-(C3-Pad1) -> Net-(C4-Pad1)
- F2 pad 1: Net-(J1-+24V) -> Net-(D1-A1)
- J1 pad 1: Net-(J1-+24V) -> Net-(D1-A1)
- J2 pad 1: +24V -> Net-(J2-Pin_1)
- J5 pad 22: +3.3V -> +5V
- J5 pad 8: +3.3V -> /Relay Board Connection/+24V_CONTACTORS
- L1 pad 2: Net-(L1-Pad2) -> Net-(C4-Pad1)
- Q1 pad 1: Net-(Q1-D) -> Net-(Q1-G)
- Q1 pad 2: Net-(Q1-G) -> GND
- Q1 pad 3: GND -> Net-(Q1-D)
- Q2 pad 1: Net-(Q2-D) -> Net-(Q2-G)
- Q2 pad 2: Net-(Q2-G) -> GND
- Q2 pad 3: GND -> Net-(Q2-D)
- Q3 pad 1: /Safety Systems/ALARM -> Net-(Q3-G)
- Q3 pad 2: Net-(Q3-G) -> GND
- Q3 pad 3: GND -> /Safety Systems/~{ALARM}
- Q4 pad 1: /STM32 Microcontroller/DMS_LATCH -> Net-(Q4-G)
- Q4 pad 2: Net-(Q4-G) -> GND
- Q4 pad 3: GND -> /STM32 Microcontroller/DMS_FAULT_LATCH
- Q5 pad 1: Net-(D18-A) -> Net-(Q5-G)
- Q5 pad 2: Net-(Q5-G) -> GND
- Q5 pad 3: GND -> Net-(D15-A)
- Q6 pad 1: Net-(Q6-D) -> Net-(Q6-G)
- Q6 pad 2: Net-(Q6-G) -> GND
- Q6 pad 3: GND -> Net-(Q6-D)
- Q7 pad 1: Net-(D19-A) -> /Safety Systems/~{ALARM}
- Q7 pad 2: /Safety Systems/ALARM -> GND
- Q7 pad 3: GND -> Net-(D16-A)
- Q8 pad 1: /Safety Systems/ALARM -> Net-(Q8-G)
- Q8 pad 2: Net-(Q8-G) -> GND
- Q8 pad 3: GND -> /Safety Systems/~{ALARM}
- R1 pad 1: Net-(C3-Pad1) -> Net-(C4-Pad1)
- R17 pad 1: /Battery Sensing/Auxiliary Battery I-V Sensing/V_SENSE -> /Battery Sensing/Auxiliary Battery I-V Sensing/5V_ISO
- R23 pad 1: /Battery Sensing/Storage Battery I-V Sensing/V_SENSE -> /Battery Sensing/Auxiliary Battery I-V Sensing/ADDR
- R23 pad 2: /Battery Sensing/Storage Battery I-V Sensing/GND_ISO -> Net-(U9B-+)
- R32 pad 1: /Safety Systems/CAN_L -> /Battery Sensing/Storage Battery I-V Sensing/GND_ISO
- R32 pad 2: /Safety Systems/CAN_H -> Net-(U13B-+)
- R49 pad 2: /STM32 Microcontroller/THROTTLE -> Net-(U28A-+)
- R52 pad 1: /STM32 Microcontroller/THROTTLE -> Net-(U28A-+)
- R55 pad 2: /STM32 Microcontroller/DMS_LATCH -> /STM32 Microcontroller/DMS_FAULT_LATCH
- R58 pad 1: /STM32 Microcontroller/DMS_LATCH -> /STM32 Microcontroller/DMS_FAULT_LATCH
- R63 pad 2: /Safety Systems/ALARM -> /Safety Systems/~{ALARM}
- R64 pad 2: /Safety Systems/ALARM -> /Safety Systems/~{ALARM}
- SW1 pad 1: /Non-Isolated Interfaces and Power/~{RST} -> Net-(R15-Pad1)
- TP1 pad 1: Net-(C3-Pad1) -> Net-(C4-Pad1)
- TP77 pad 1: /Safety Systems/CAN_H -> Net-(TP77-Pad1)
- TP82 pad 1: /STM32 Microcontroller/THROTTLE -> Net-(U28A-+)
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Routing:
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- added copper zone on B.Cu, net GND
- added copper zone on F.Cu, net GND
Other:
- board text added: "INVERT TEMP and NETWORK CONNECTORS?"

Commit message: power-pcb: finish placement and started routing
Started routing power traces only and didn't place test points yet.
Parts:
- JP6, R19, R39, R40, R69, R70: moved to B.Cu
- R1, R14, R2: footprint Resistor_SMD:R_0603_1608Metric_Pad0.98x0.95mm_HandSolder -> Resistor_SMD:R_0805_2012Metric_Pad1.20x1.40mm_HandSolder
- R10, R22, R23, R24, R25, R31, R32, R33, R34, R41, R42, R43, R46, R47, R51, R53, R54, R55, R56, R57, R58, R59, R60, R61, R62, R66, R67, R68: value 10k -> 12k; footprint Resistor_SMD:R_0603_1608Metric_Pad0.98x0.95mm_HandSolder -> Resistor_SMD:R_0402_1005Metric_Pad0.72x0.64mm_HandSolder
- R16, R4: footprint Resistor_SMD:R_0402_1005Metric_Pad0.72x0.64mm_HandSolder -> Resistor_SMD:R_0603_1608Metric_Pad0.98x0.95mm_HandSolder
- moved TP43 366.1 mm to (-64.9, 129.7)
- moved TP44 366.1 mm to (-73.0, 139.2)
- moved TP45 366.1 mm to (-64.9, 133.2)
- moved TP46 366.1 mm to (-68.5, 138.7)
- moved TP47 366.1 mm to (-73.0, 144.2)
- moved TP48 366.1 mm to (-68.5, 142.8)
- moved TP50 363.2 mm to (-63.5, 171.7)
- moved TP52 363.2 mm to (-63.5, 175.2)
- moved TP72 353.4 mm to (-76.8, 115.3)
- moved TP73 353.4 mm to (-76.8, 120.4)
- moved TP74 353.4 mm to (-76.8, 125.5)
- moved TP75 353.4 mm to (-76.8, 130.5)
- moved TP51 349.1 mm to (-59.8, 137.2)
- moved TP53 349.1 mm to (-55.2, 136.7)
- moved TP54 349.1 mm to (-59.8, 142.2)
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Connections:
- D9 pad 1: +24V -> Net-(D9-A1)
- F3 pad 2: Net-(J2-Pin_1) -> Net-(D9-A1)
- J2 pad 1: Net-(J2-Pin_1) -> Net-(D9-A1)
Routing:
- net +5V: track 0.00 -> 327.6 mm, vias 0 -> 8
- net /Relay Board Connection/+24V_CONTACTORS: track 0.00 -> 56.9 mm
- net /Battery Sensing/Storage Battery I-V Sensing/5V_ISO: track 0.00 -> 54.6 mm
- net /Battery Sensing/Auxiliary Battery I-V Sensing/5V_ISO: track 0.00 -> 51.0 mm
- net /Non-Isolated Interfaces and Power/USB_D+: track 46.2 -> 0.00 mm
- net /Non-Isolated Interfaces and Power/USB_D-: track 46.2 -> 0.00 mm
- net /Isolated Interfaces/5V_FC: track 0.00 -> 36.7 mm, vias 0 -> 1
- net /Non-Isolated Interfaces and Power/5V_USB: track 0.00 -> 30.6 mm
- net /Isolated Interfaces/Charge Controller Isolated UART/+Viso: track 0.00 -> 30.5 mm, vias 0 -> 1
- net /Isolated Interfaces/Storage Battery Isolated UART/+Viso: track 0.00 -> 28.4 mm, vias 0 -> 1
- net /Non-Isolated Interfaces and Power/PC_D-: track 23.7 -> 0.91 mm, vias 1 -> 0
- net /Non-Isolated Interfaces and Power/PC_D+: track 22.8 -> 0.91 mm, vias 1 -> 0
- net GND: track 0.00 -> 16.2 mm, vias 0 -> 1
- net /Isolated Interfaces/FC_D+: track 14.2 -> 2.83 mm
- net /Isolated Interfaces/FC_D-: track 13.4 -> 2.64 mm
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- added copper zone on F.Cu, net +24V
- added copper zone on B.Cu, net /Battery Sensing/Auxiliary Battery I-V Sensing/ADDR
- added copper zone on F.Cu, net /Battery Sensing/Auxiliary Battery I-V Sensing/ADDR
- added copper zone on B.Cu, net /Battery Sensing/Storage Battery I-V Sensing/GND_ISO
- added copper zone on F.Cu, net /Battery Sensing/Storage Battery I-V Sensing/GND_ISO
- added copper zone on B.Cu, net /Isolated Interfaces/Charge Controller Isolated UART/-Viso
- added copper zone on F.Cu, net /Isolated Interfaces/Charge Controller Isolated UART/-Viso
- added copper zone on B.Cu, net /Isolated Interfaces/GND_FC
- added copper zone on F.Cu, net /Isolated Interfaces/GND_FC
- added copper zone on B.Cu, net /Isolated Interfaces/Storage Battery Isolated UART/-Viso
- added copper zone on F.Cu, net /Isolated Interfaces/Storage Battery Isolated UART/-Viso
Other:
- board text added: "GND"
- board text removed: "INVERT TEMP and NETWORK CONNECTORS?"
